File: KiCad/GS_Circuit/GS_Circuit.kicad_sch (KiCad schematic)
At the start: 13 parts, among them J1 AVR-ISP-6, SW1 SW_Push, SW2 SW_SPST, U2 ATtiny85V-10P

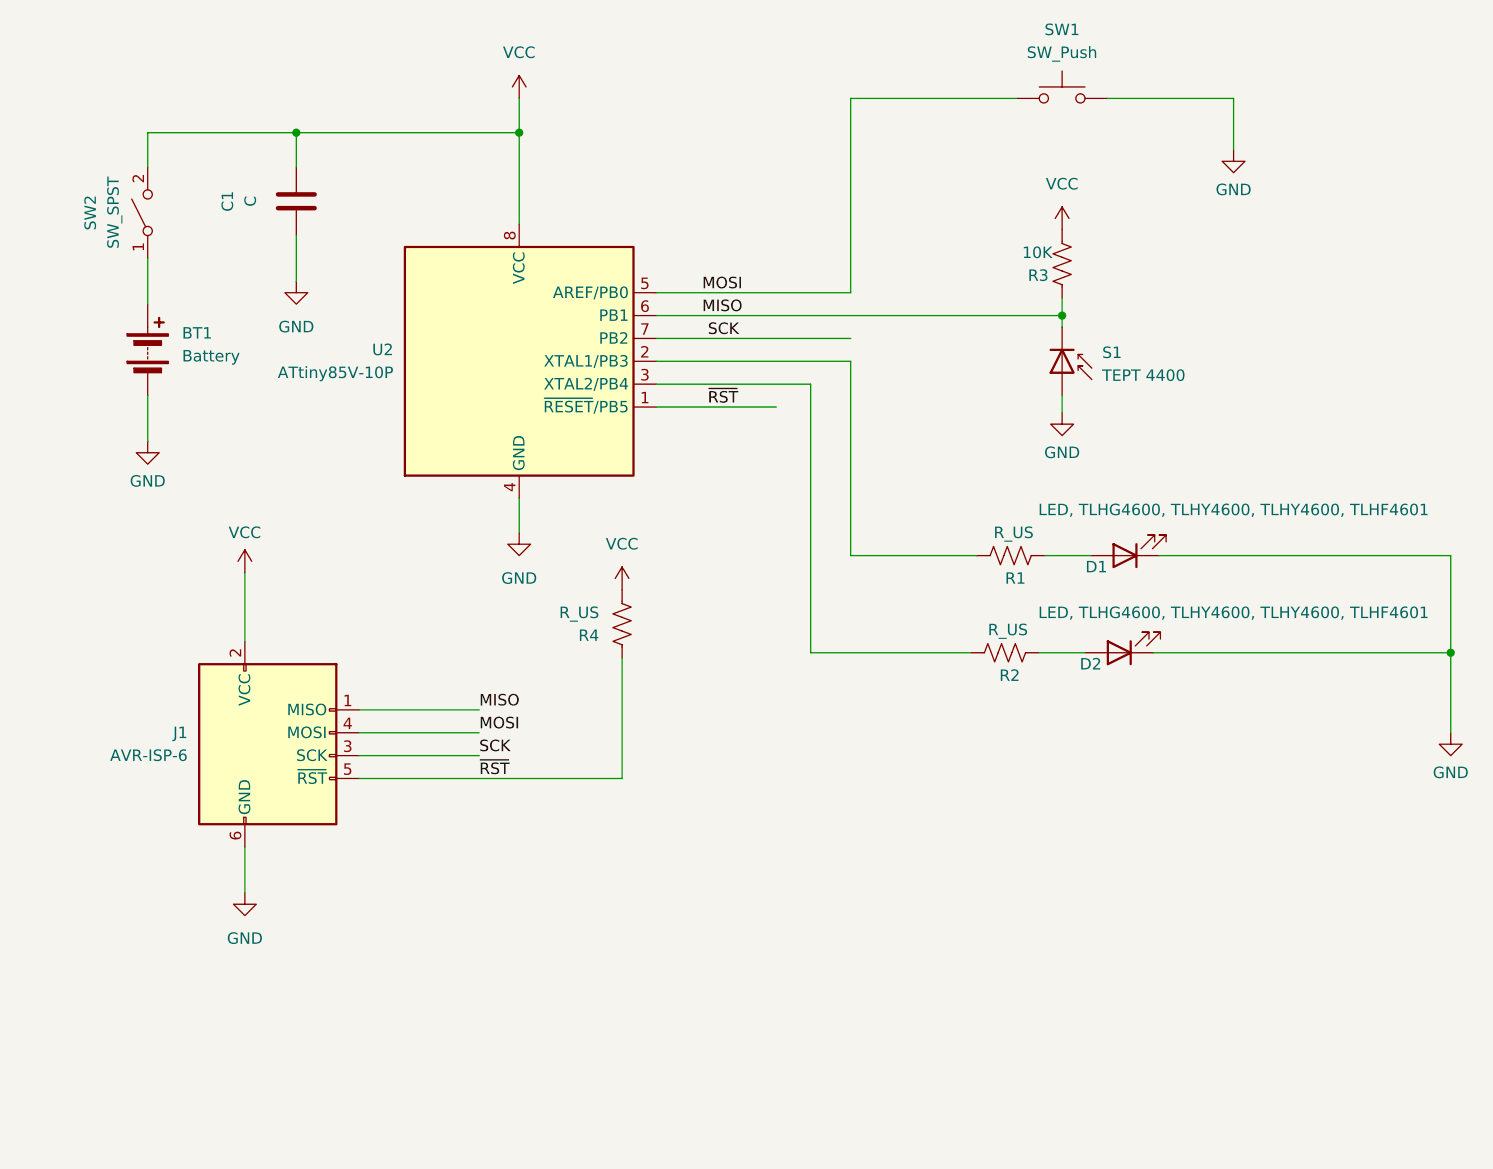
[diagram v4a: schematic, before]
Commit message: MD e-negative feedback 2
- Moved capacitor & rotate
- Updated foot prints for LEDS
- Added BOM
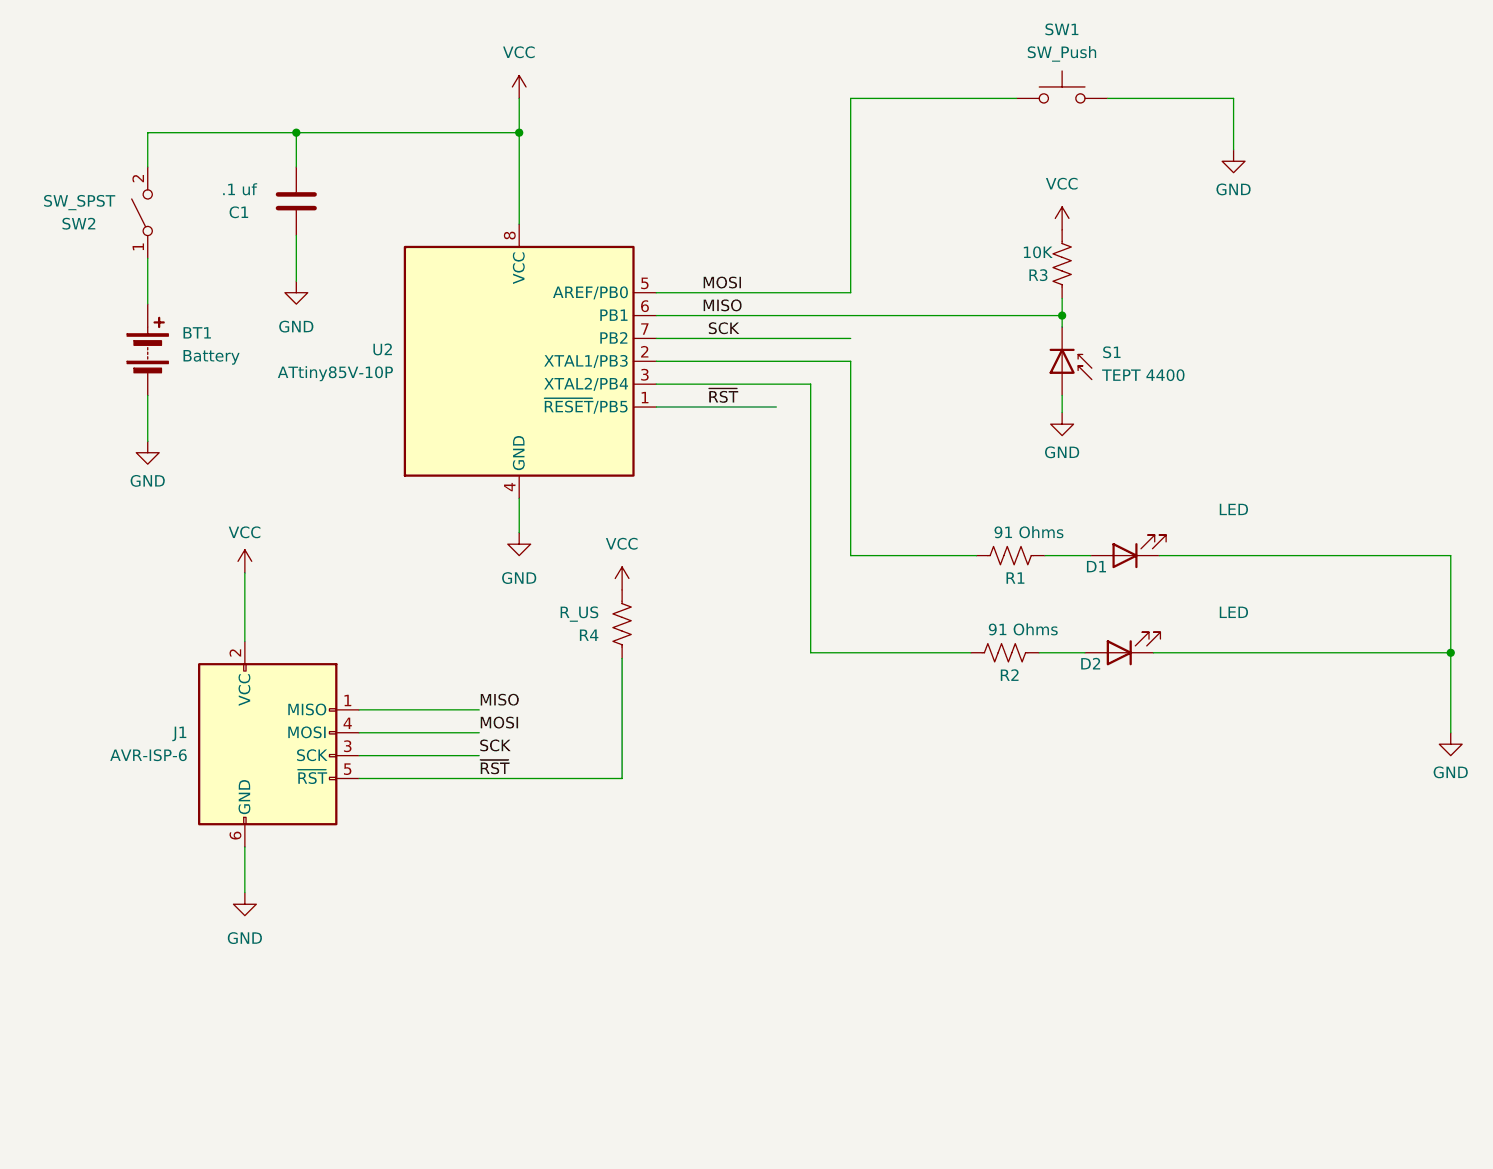
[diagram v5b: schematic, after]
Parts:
- C1: value C -> .1 uf
- D1, D2: value LED, TLHG4600, TLHY4600, TLHY4600, TLHF4601 -> LED; footprint LED_THT:LED_D3.0mm -> GS_Parts:LED_D5.0mm; DIGIKEY (none) -> 1516-QBL8IW60D-CW-ND, 1516-1364-ND, 754-1888-ND, 67-2288-ND
- R1, R2: value R_US -> 91 Ohms
- S1: footprint GS_Parts:TEPT4400 -> GS_Parts:THT_TEPT4400
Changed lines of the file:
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@@
 			)
 		)
-		(property "Footprint" "GS_Parts:TEPT4400"
+		(property "Footprint" "GS_Parts:THT_TEPT4400"
 			(at 131.445 58.42 0)
 			(effects
@@
 		(property "Description" "Photodiode"
 			(at 131.445 59.69 0)
+			(effects
+				(font
+					(size 1.27 1.27)
+				)
+				(hide yes)
+			)
+		)
+		(property "DIGIKEY" ""
+			(at 131.445 59.69 90)
 			(effects
 				(font
@@
 		(dnp no)
 		(property "Reference" "SW2"
-			(at 23.495 41.91 0)
+			(at 22.225 43.18 90)
 			(effects
 				(font
@@
 		)
 		(property "Value" "SW_SPST"
-			(at 26.035 41.91 0)
+			(at 22.225 40.64 90)
 			(effects
 				(font
@@
 		(property "Description" "Single Pole Single Throw (SPST) switch"
 			(at 29.845 41.91 0)
+			(effects
+				(font
+					(size 1.27 1.27)
+				)
+				(hide yes)
+			)
+		)
+		(property "DIGIKEY" ""
+			(at 29.845 41.91 90)
 			(effects
 				(font
@@
 		(dnp no)
 		(property "Reference" "C1"
-			(at 38.735 40.64 90)
-			(effects
-				(font
-					(size 1.27 1.27)
-				)
-			)
-		)
-		(property "Value" "C"
-			(at 41.275 40.64 90)
+			(at 40.005 41.91 0)
+			(effects
+				(font
+					(size 1.27 1.27)
+				)
+			)
+		)
+		(property "Value" ".1 uf"
+			(at 40.005 39.37 0)
 			(effects
 				(font
@@
 		)
 		(property "Description" "Unpolarized capacitor"
+			(at 46.355 40.64 0)
+			(effects
+				(font
+					(size 1.27 1.27)
+				)
+				(hide yes)
+			)
+		)
+		(property "DIGIKEY" ""
 			(at 46.355 40.64 0)
 			(effects
@@
 			)
 		)
+		(property "DIGIKEY" ""
+			(at 131.445 29.21 0)
+			(effects
+				(font
+					(size 1.27 1.27)
+				)
+				(hide yes)
+			)
+		)
 		(pin "2"
 		)
@@
 			)
 		)
-		(property "Value" "LED, TLHG4600, TLHY4600, TLHY4600, TLHF4601"
+		(property "Value" "LED"
 			(at 150.495 86.36 0)
 			(effects
@@
 			)
 		)
-		(property "Footprint" "LED_THT:LED_D3.0mm"
+		(property "Footprint" "GS_Parts:LED_D5.0mm"
 			(at 137.795 90.805 0)
 			(effects
@@
 			)
 		)
+		(property "DIGIKEY" "1516-QBL8IW60D-CW-ND,   1516-1364-ND,   754-1888-ND,   67-2288-ND"
+			(at 137.795 90.805 0)
+			(effects
+				(font
+					(size 1.27 1.27)
+				)
+				(hide yes)
+			)
+		)
 		(pin "1"
 		)
@@
 			)
 		)
-		(property "Value" "R_US"
+		(property "Value" "91 Ohms"
 			(at 123.19 88.265 90)
 			(effects
@@
 		(property "Description" "Resistor, US symbol"
 			(at 125.095 90.805 0)
+			(effects
+				(font
+					(size 1.27 1.27)
+				)
+				(hide yes)
+			)
+		)
+		(property "DIGIKEY" ""
+			(at 125.095 90.805 90)
 			(effects
 				(font
@@
 			)
 		)
-		(property "Value" "R_US"
+		(property "Value" "91 Ohms"
 			(at 123.825 77.47 90)
 			(effects
@@
 		(property "Description" "Resistor, US symbol"
 			(at 125.73 80.01 0)
+			(effects
+				(font
+					(size 1.27 1.27)
+				)
+				(hide yes)
+			)
+		)
+		(property "DIGIKEY" ""
+			(at 125.73 80.01 90)
 			(effects
 				(font
@@
 			)
 		)
+		(property "DIGIKEY" ""
+			(at 43.18 102.235 0)
+			(effects
+				(font
+					(size 1.27 1.27)
+				)
+				(hide yes)
+			)
+		)
 		(pin "5"
 		)
@@
 			)
 		)
+		(property "DIGIKEY" ""
+			(at 131.445 47.625 0)
+			(effects
+				(font
+					(size 1.27 1.27)
+				)
+				(hide yes)
+			)
+		)
 		(pin "2"
 		)
@@
 			)
 		)
-		(property "Value" "LED, TLHG4600, TLHY4600, TLHY4600, TLHF4601"
+		(property "Value" "LED"
 			(at 150.495 74.93 0)
 			(effects
@@
 			)
 		)
-		(property "Footprint" "LED_THT:LED_D3.0mm"
+		(property "Footprint" "GS_Parts:LED_D5.0mm"
 			(at 138.43 80.01 0)
 			(effects
@@
 		)
 		(property "Sim.Pins" "1=K 2=A"
+			(at 138.43 80.01 0)
+			(effects
+				(font
+					(size 1.27 1.27)
+				)
+				(hide yes)
+			)
+		)
+		(property "DIGIKEY" "1516-QBL8IW60D-CW-ND,   1516-1364-ND,   754-1888-ND,   67-2288-ND"
 			(at 138.43 80.01 0)
 			(effects
@@
 			)
 		)
+		(property "DIGIKEY" ""
+			(at 29.845 57.15 0)
+			(effects
+				(font
+					(size 1.27 1.27)
+				)
+				(hide yes)
+			)
+		)
 		(pin "2"
 		)
@@
 			)
 		)
+		(property "DIGIKEY" ""
+			(at 71.12 58.42 0)
+			(effects
+				(font
+					(size 1.27 1.27)
+				)
+				(hide yes)
+			)
+		)
 		(pin "5"
 		)
@@
 			(at 82.55 87.63 0)
 			(effects
+				(font
+					(size 1.27 1.27)
+				)
+				(hide yes)
+			)
+		)
+		(property "DIGIKEY" ""
+			(at 82.55 87.63 0)
+			(effects

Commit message: Loose Saves
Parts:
- BT1: DIGIKEY (none) -> 36-2464-ND
- R4: value R_US -> 10K
- S1: DIGIKEY (none) -> 751-1057-ND
- U2: DIGIKEY (none) -> ATTINY85-20PU-ND
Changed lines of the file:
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@@
 			)
 		)
-		(property "DIGIKEY" ""
+		(property "DIGIKEY" "  751-1057-ND"
 			(at 131.445 59.69 90)
 			(effects
@@
 			)
 		)
-		(property "DIGIKEY" ""
+		(property "DIGIKEY" "36-2464-ND"
 			(at 29.845 57.15 0)
 			(effects
@@
 			)
 		)
-		(property "DIGIKEY" ""
+		(property "DIGIKEY" "ATTINY85-20PU-ND"
 			(at 71.12 58.42 0)
 			(effects
@@
 			)
 		)
-		(property "Value" "R_US"
+		(property "Value" "10K"
 			(at 80.01 86.3601 0)
 			(effects

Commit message: MD E Feeback 3
Moved Lights
Horizontal/Vertical Wiring
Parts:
- SW1: DIGIKEY (none) -> EG5888-ND
- SW2: DIGIKEY (none) -> EG5886-ND
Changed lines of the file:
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@@
 			)
 		)
-		(property "DIGIKEY" ""
+		(property "DIGIKEY" "EG5886-ND"
 			(at 29.845 41.91 90)
 			(effects
@@
 			)
 		)
-		(property "DIGIKEY" ""
+		(property "DIGIKEY" "EG5888-ND"
 			(at 131.445 29.21 0)
 			(effects

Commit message: Rev 1 as built
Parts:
- added XX1: White LED, symbol tens:BOM_item
- added XX2: Green LED, symbol tens:BOM_item
- added XX3: Red LED, symbol tens:BOM_item
- added XX4: Blue LED, symbol tens:BOM_item
- added XX5: DIP-8 Socket, symbol tens:BOM_item
- added XX6: Cap Red, symbol tens:BOM_item
- added XX7: Cap Blue, symbol tens:BOM_item
- C1: DIGIKEY (none) -> 445-173588-1-ND
- D1, D2: DIGIKEY 1516-QBL8IW60D-CW-ND, 1516-1364-ND, 754-1888-ND, 67-2288-ND -> Various; now left out of the parts list
- J1: now not fitted; now left out of the parts list
- R1, R2: DIGIKEY (none) -> CF14JT91R0CT-ND
- R3, R4: DIGIKEY (none) -> CF14JT10K0CT-ND
- S1: DIGIKEY 751-1057-ND -> 751-1057-ND
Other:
- note added: "Additional BOM Items"
